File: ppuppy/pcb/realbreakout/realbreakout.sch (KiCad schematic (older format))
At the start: 6 parts, among them J1 Conn_01x36, J2 Conn_01x36, J3 Conn_01x36, U1 nescartheader, U2 piheader

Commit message: More notes, work on breakout; add gpio 'direct access' code that is supposedly faster than bcm lib (but actually it appears to use the same approach, maybe without memory barrier)?
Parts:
- added U?: nescic, symbol nescic
- E1: renamed from E?; footprint (none) -> Housings_DIP:DIP-32_W15.24mm
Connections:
- net 5V: now also U?.16 (5V)
- net GND: now also U?.11 (GND/RESET_A), U?.12 (GND/RESET_B), U?.13 (GND), U?.14 (GND), U?.15 (GND), U?.3 (SEED), U?.4 (LOCK_KEY), U?.8 (GND)
- net at J1.34 (Pin_34), U1.34 (CIC_toPak): now also U?.2 (DATA_IN)
- net at J1.35 (Pin_35), U1.35 (CIC_toMB): now also U?.1 (DATA_OUT)
- net at J2.3 (Pin_3), J3.3 (Pin_3), U1.70 (/CIC_RST): now also U?.7 (RESET)
- net at J2.2 (Pin_2), J3.2 (Pin_2), U1.71 (CIC_CLK): now also U?.6 (CLK)

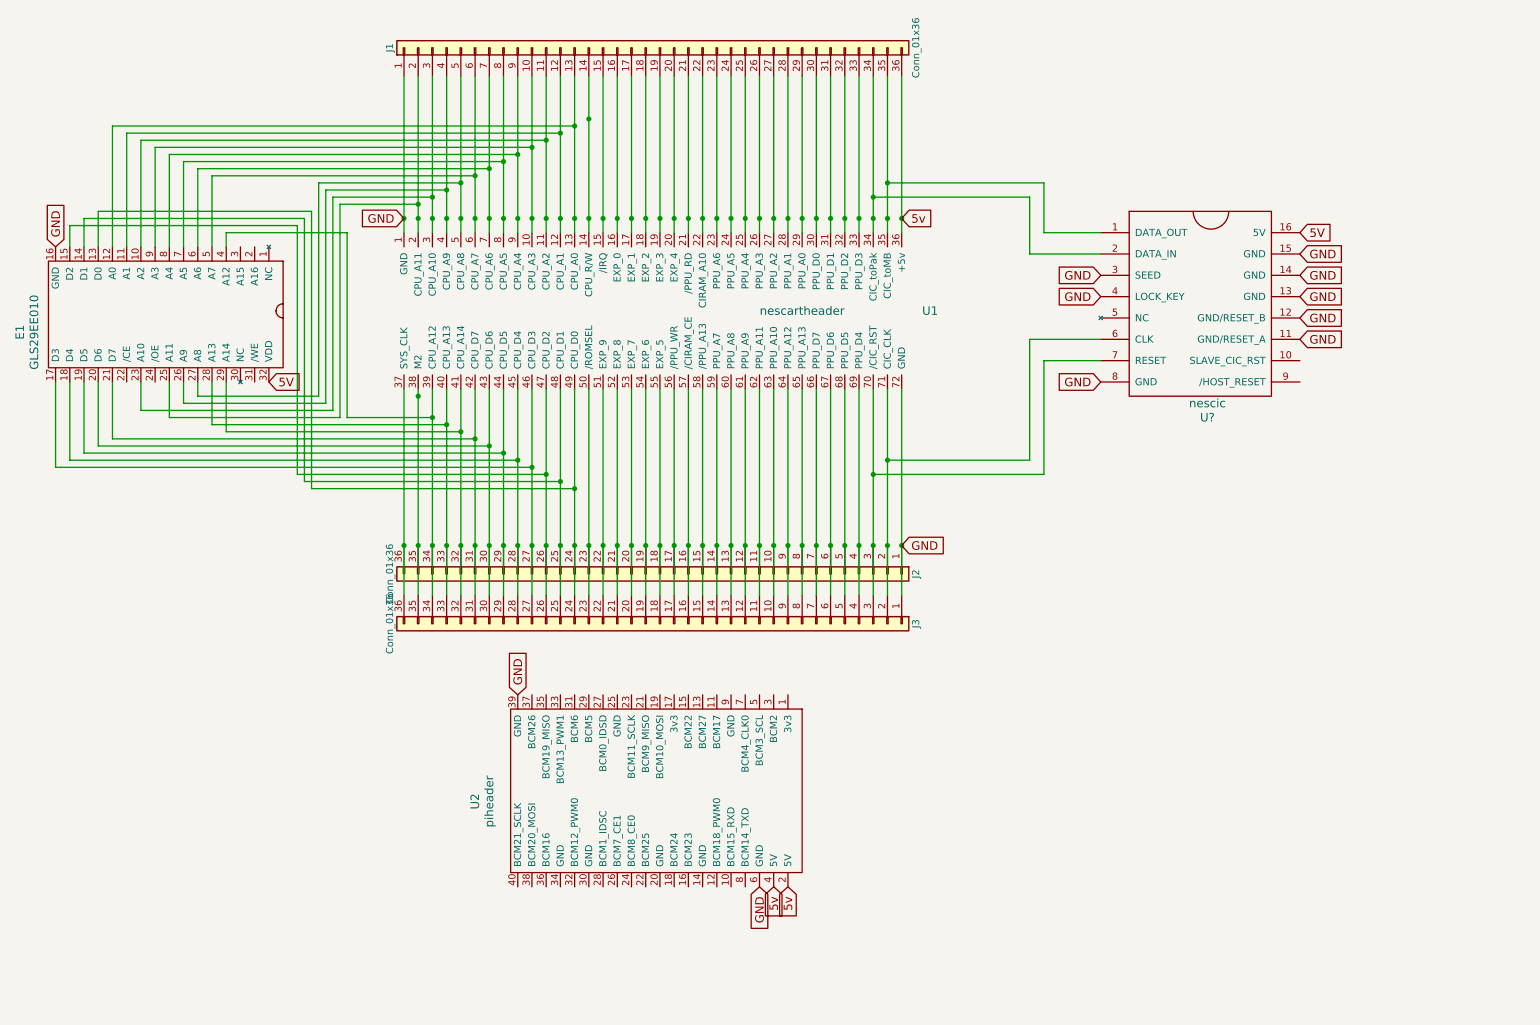
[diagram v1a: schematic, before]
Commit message: Almost ready PCB, longer lead-in in cart knock
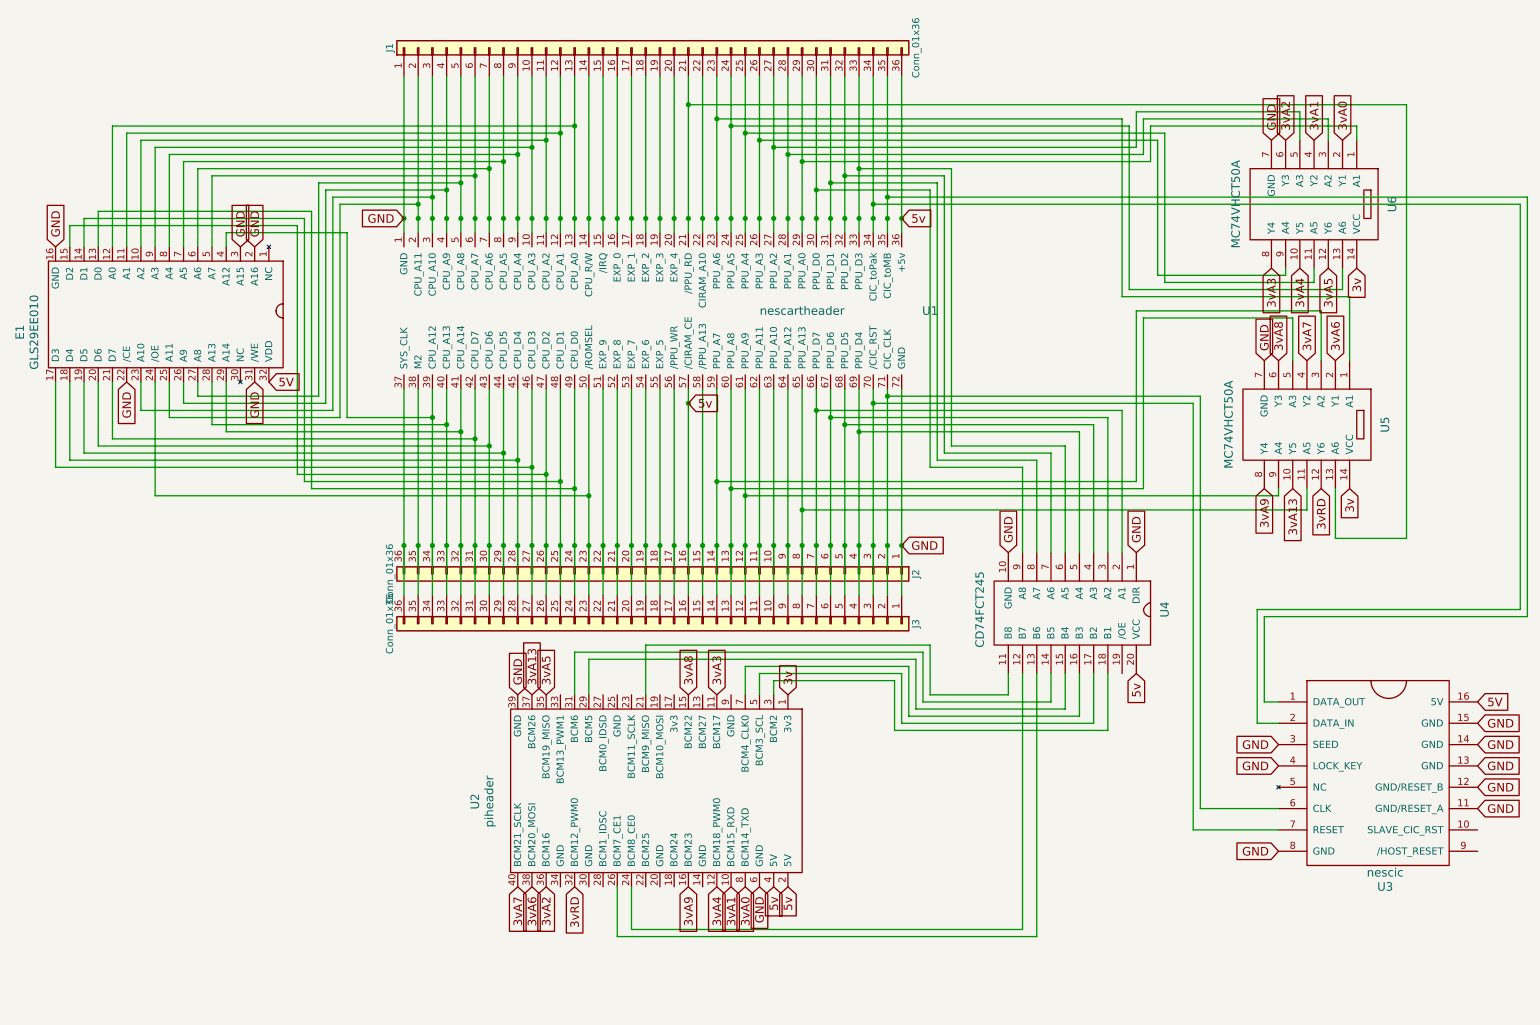
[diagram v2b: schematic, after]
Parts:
- added U4: CD74FCT245, Housings_DIP:DIP-20_W7.62mm, symbol CD74FCT245
- added U5, U6: MC74VHCT50A, Housings_SOIC:SOIC-14_3.9x8.7mm_Pitch1.27mm, symbol MC74VHCT50A
- U3: renamed from U?; footprint (none) -> Housings_DIP:DIP-16_W7.62mm
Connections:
- net 5v: now also J2.16 (Pin_16), J3.16 (Pin_16), U1.57 (/CIRAM_CE), U4.20 (VCC)
- net GND: now also E1.2 (A16), E1.22 (/CE), E1.3 (A15), E1.31 (/WE), U4.1 (DIR), U4.10 (GND), U5.7 (GND), U6.7 (GND)
- net at J1.21 (Pin_21), U1.21 (/PPU_RD): now also U5.13 (A6)
- net at J1.23 (Pin_23), U1.23 (PPU_A6): now also U5.1 (A1)
- net at J1.24 (Pin_24), U1.24 (PPU_A5): now also U6.13 (A6)
- net at J1.25 (Pin_25), U1.25 (PPU_A4): now also U6.11 (A5)
- net at J1.26 (Pin_26), U1.26 (PPU_A3): now also U6.9 (A4)
- net at J1.27 (Pin_27), U1.27 (PPU_A2): now also U6.5 (A3)
- net at J1.28 (Pin_28), U1.28 (PPU_A1): now also U6.3 (A2)
- net at J1.29 (Pin_29), U1.29 (PPU_A0): now also U6.1 (A1)
- net at J1.30 (Pin_30), U1.30 (PPU_D0): now also U4.9 (A8)
- net at J1.31 (Pin_31), U1.31 (PPU_D1): now also U4.8 (A7)
- net at J1.32 (Pin_32), U1.32 (PPU_D2): now also U4.7 (A6)
- net at J1.33 (Pin_33), U1.33 (PPU_D3): now also U4.6 (A5)
- net at J2.23 (Pin_23), J3.23 (Pin_23), U1.50 (/ROMSEL): now also E1.24 (/OE)
- net at J2.14 (Pin_14), J3.14 (Pin_14), U1.59 (PPU_A7): now also U5.3 (A2)
- net at J2.13 (Pin_13), J3.13 (Pin_13), U1.60 (PPU_A8): now also U5.5 (A3)
- net at J2.12 (Pin_12), J3.12 (Pin_12), U1.61 (PPU_A9): now also U5.9 (A4)
- net at J2.8 (Pin_8), J3.8 (Pin_8), U1.65 (PPU_A13): now also U5.11 (A5)
- net at J2.7 (Pin_7), J3.7 (Pin_7), U1.66 (PPU_D7): now also U4.2 (A1)
- net at J2.6 (Pin_6), J3.6 (Pin_6), U1.67 (PPU_D6): now also U4.3 (A2)
- net at J2.5 (Pin_5), J3.5 (Pin_5), U1.68 (PPU_D5): now also U4.4 (A3)
- net at J2.4 (Pin_4), J3.4 (Pin_4), U1.69 (PPU_D4): now also U4.5 (A4)
- net 3v: now reaches U2.1 (3v3)
- net 3v: now also U5.14 (VCC), U6.14 (VCC)
- net 3vA1: now reaches U2.10 (BCM15_RXD)
- net 3vA1: now also U6.4 (Y2)
- net 3vA3: now reaches U2.11 (BCM17)
- net 3vA3: now also U6.8 (Y4)
- net 3vA4: now reaches U2.12 (BCM18_PWM0)
- net 3vA4: now also U6.10 (Y5)
- net 3vA8: now reaches U2.15 (BCM22)
- net 3vA8: now also U5.6 (Y3)
- net 3vA9: now reaches U2.16 (BCM23)
- net 3vA9: now also U5.8 (Y4)
- net at U2.21 (BCM9_MISO): now also U4.11 (B8)
- net at U2.24 (BCM8_CE0): now also U4.12 (B7)
- net at U2.26 (BCM7_CE1): now also U4.13 (B6)
- net at U2.29 (BCM5): now also U4.15 (B4)
- net at U2.3 (BCM2): now also U4.18 (B1)
- net at U2.31 (BCM6): now also U4.14 (B5)
- net 3vRD: now reaches U2.32 (BCM12_PWM0)
- net 3vRD: now also U5.12 (Y6)
- net 3vA5: now reaches U2.35 (BCM19_MISO)
- net 3vA5: now also U6.12 (Y6)
- net 3vA2: now reaches U2.36 (BCM16)
- net 3vA2: now also U6.6 (Y3)
- net 3vA13: now reaches U2.37 (BCM26)
- net 3vA13: now also U5.10 (Y5)
- net 3vA6: now reaches U2.38 (BCM20_MOSI)
- net 3vA6: now also U5.2 (Y1)
- net 3vA7: now reaches U2.40 (BCM21_SCLK)
- net 3vA7: now also U5.4 (Y2)
- net at U2.5 (BCM3_SCL): now also U4.17 (B2)
- net at U2.7 (BCM4_CLK0): now also U4.16 (B3)
- net 3vA0: now reaches U2.8 (BCM14_TXD)
- net 3vA0: now also U6.2 (Y1)
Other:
- moved on the sheet: U3

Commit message: This is the version of PCB that I first printed
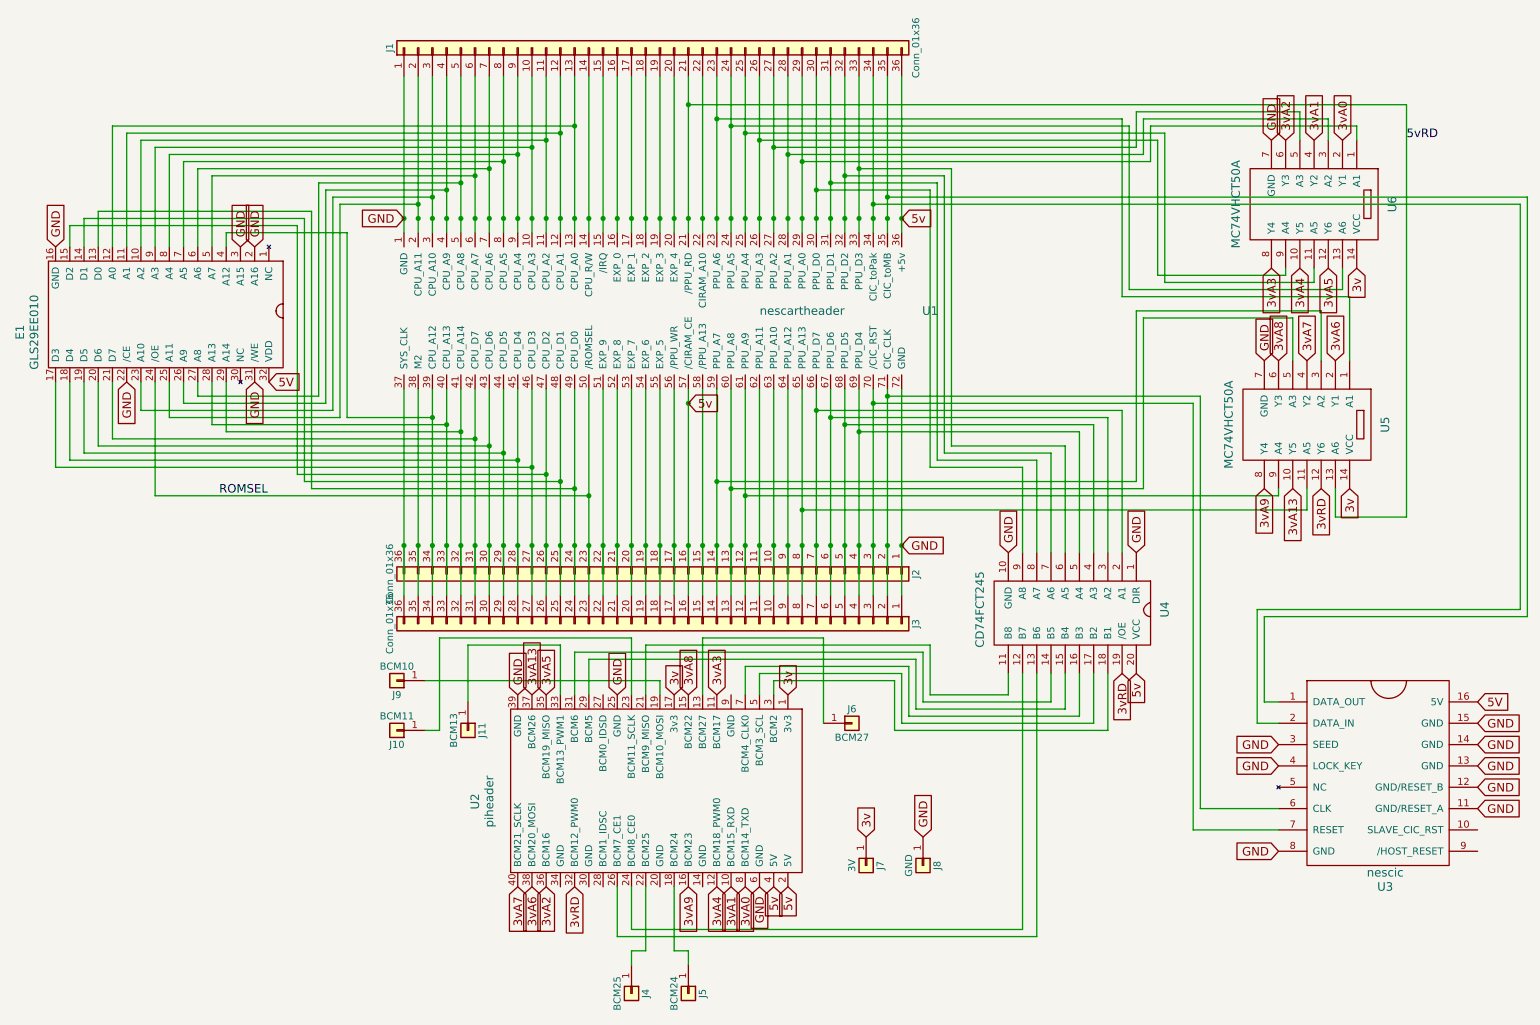
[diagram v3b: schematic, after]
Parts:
- added J10: BCM11, symbol Conn_01x01
- added J11: BCM13, symbol Conn_01x01
- added J4: BCM25, Pin_Headers:Pin_Header_Straight_1x01_Pitch2.54mm, symbol Conn_01x01
- added J5: BCM24, Pin_Headers:Pin_Header_Straight_1x01_Pitch2.54mm, symbol Conn_01x01
- added J6: BCM27, Pin_Headers:Pin_Header_Straight_1x01_Pitch2.54mm, symbol Conn_01x01
- added J7: 3V, Pin_Headers:Pin_Header_Straight_1x01_Pitch2.54mm, symbol Conn_01x01
- added J8: GND, Pin_Headers:Pin_Header_Straight_1x01_Pitch2.54mm, symbol Conn_01x01
- added J9: BCM10, symbol Conn_01x01
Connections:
- net 3v: now also U2.17 (3v3), J7.1 (Pin_1)
- net 3vRD: now also U4.19 (/OE)
- net GND: now also U2.25 (GND), J8.1 (Pin_1)
- net 5vRD: now reaches J1.21 (Pin_21), U1.21 (/PPU_RD), U5.13 (A6)
- net ROMSEL: now reaches E1.24 (/OE), J2.23 (Pin_23), J3.23 (Pin_23), U1.50 (/ROMSEL)
- net at U2.13 (BCM27): now also J6.1 (Pin_1)
- net at U2.18 (BCM24): now also J5.1 (Pin_1)
- net at U2.19 (BCM10_MOSI): now also J9.1 (Pin_1)
- net at U2.22 (BCM25): now also J4.1 (Pin_1)
- net at U2.23 (BCM11_SCLK): now also J10.1 (Pin_1)
- net at U2.33 (BCM13_PWM1): now also J11.1 (Pin_1)
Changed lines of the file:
@@
 Wire Wire Line
 	5200 550  10250 550
-Wire Wire Line
-	10250 550  10250 3600
-Wire Wire Line
-	10250 3600 9750 3600
-Wire Wire Line
-	9750 3600 9750 3250
 Text GLabel 9650 3250 3    60   Input ~ 0
 3vRD
@@
 Text GLabel 5200 2650 2    60   Input ~ 0
 5v
+Text GLabel 4700 4700 1    60   Input ~ 0
+GND
+Text GLabel 5100 4700 1    60   Input ~ 0
+3v
+Text GLabel 8250 4550 3    60   Input ~ 0
+3vRD
+Wire Wire Line
+	10250 550  10250 3450
+Wire Wire Line
+	10250 3450 9750 3450
+Wire Wire Line
+	9750 3450 9750 3250
+Text Label 10250 800  0    60   ~ 0
+5vRD
+Text Label 1900 3300 0    60   ~ 0
+ROMSEL
+$Comp
+L Conn_01x01 J5
+U 1 1 5ADD43A7
+P 5200 6800
+F 0 "J5" H 5200 6900 50  0000 C CNN
+F 1 "BCM24" H 5200 6700 50  0000 C CNN
+F 2 "Pin_Headers:Pin_Header_Straight_1x01_Pitch2.54mm" H 5200 6800 50  0001 C CNN
+F 3 "" H 5200 6800 50  0001 C CNN
+	1    5200 6800
+	0    1    1    0
+$EndComp
+$Comp
+L Conn_01x01 J4
+U 1 1 5ADD45DE
+P 4800 6800
+F 0 "J4" H 4800 6900 50  0000 C CNN
+F 1 "BCM25" H 4800 6700 50  0000 C CNN
+F 2 "Pin_Headers:Pin_Header_Straight_1x01_Pitch2.54mm" H 4800 6800 50  0001 C CNN
+F 3 "" H 4800 6800 50  0001 C CNN
+	1    4800 6800
+	0    1    1    0
+$EndComp
+Wire Wire Line
+	4900 6050 4900 6500
+Wire Wire Line
+	4900 6500 4800 6500
+Wire Wire Line
+	4800 6500 4800 6600
+Wire Wire Line
+	5100 6050 5100 6500
+Wire Wire Line
+	5100 6500 5200 6500
+Wire Wire Line
+	5200 6500 5200 6600
+$Comp
+L Conn_01x01 J6
+U 1 1 5ADD4C20
+P 6350 4900
+F 0 "J6" H 6350 5000 50  0000 C CNN
+F 1 "BCM27" H 6350 4800 50  0000 C CNN
+F 2 "Pin_Headers:Pin_Header_Straight_1x01_Pitch2.54mm" H 6350 4900 50  0001 C CNN
+F 3 "" H 6350 4900 50  0001 C CNN
+	1    6350 4900
+	1    0    0    -1
+$EndComp
+Wire Wire Line
+	6150 4900 6150 4300
+Wire Wire Line
+	6150 4300 5300 4300
+Wire Wire Line
+	5300 4300 5300 4700
+$Comp
+L Conn_01x01 J7
+U 1 1 5ADD4DE4
+P 6450 5900
+F 0 "J7" H 6450 6000 50  0000 C CNN
+F 1 "3V" H 6450 5800 50  0000 C CNN
+F 2 "Pin_Headers:Pin_Header_Straight_1x01_Pitch2.54mm" H 6450 5900 50  0001 C CNN
+F 3 "" H 6450 5900 50  0001 C CNN
+	1    6450 5900
+	0    1    1    0
+$EndComp
+$Comp
+L Conn_01x01 J8
+U 1 1 5ADD4E5F
+P 6850 5900
+F 0 "J8" H 6850 6000 50  0000 C CNN
+F 1 "GND" H 6850 5800 50  0000 C CNN
+F 2 "Pin_Headers:Pin_Header_Straight_1x01_Pitch2.54mm" H 6850 5900 50  0001 C CNN
+F 3 "" H 6850 5900 50  0001 C CNN
+	1    6850 5900
+	0    1    1    0
+$EndComp
+Text GLabel 6850 5700 1    60   Input ~ 0
+GND
+Text GLabel 6450 5700 1    60   Input ~ 0
+3v
+$Comp
+L Conn_01x01 J11
+U 1 1 5ADD5E6F
+P 3650 4950
+F 0 "J11" H 3650 5050 50  0000 C CNN
+F 1 "BCM13" H 3650 4850 50  0000 C CNN
+F 2 "" H 3650 4950 50  0001 C CNN
+F 3 "" H 3650 4950 50  0001 C CNN
+	1    3650 4950
+	0    1    1    0
+$EndComp
+Wire Wire Line
+	3650 4750 3650 4350
+Wire Wire Line
+	3650 4350 4300 4350
+Wire Wire Line
+	4300 4350 4300 4700
+$Comp
+L Conn_01x01 J9
+U 1 1 5ADD629E
+P 3150 4600
+F 0 "J9" H 3150 4700 50  0000 C CNN
+F 1 "BCM10" H 3150 4500 50  0000 C CNN
+F 2 "" H 3150 4600 50  0001 C CNN
+F 3 "" H 3150 4600 50  0001 C CNN
+	1    3150 4600
+	-1   0    0    1
+$EndComp
+$Comp
+L Conn_01x01 J10
+U 1 1 5ADD6490
+P 3150 4950
+F 0 "J10" H 3150 5050 50  0000 C CNN
+F 1 "BCM11" H 3150 4850 50  0000 C CNN
+F 2 "" H 3150 4950 50  0001 C CNN
+F 3 "" H 3150 4950 50  0001 C CNN
+	1    3150 4950
+	-1   0    0    1
+$EndComp
+Wire Wire Line
+	3350 4950 3450 4950
+Wire Wire Line
+	3450 4950 3450 4300
+Wire Wire Line
+	3450 4300 4800 4300
+Wire Wire Line
+	4800 4300 4800 4700
+Wire Wire Line
+	3350 4600 5000 4600
+Wire Wire Line
+	5000 4600 5000 4700
 $EndSCHEMATC

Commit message: v2 of board
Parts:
- J10, J11, J9: footprint (none) -> Pin_Headers:Pin_Header_Straight_1x01_Pitch2.54mm
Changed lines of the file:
@@
 F 0 "J11" H 3650 5050 50  0000 C CNN
 F 1 "BCM13" H 3650 4850 50  0000 C CNN
-F 2 "" H 3650 4950 50  0001 C CNN
+F 2 "Pin_Headers:Pin_Header_Straight_1x01_Pitch2.54mm" H 3650 4950 50  0001 C CNN
 F 3 "" H 3650 4950 50  0001 C CNN
 	1    3650 4950
@@
 F 0 "J9" H 3150 4700 50  0000 C CNN
 F 1 "BCM10" H 3150 4500 50  0000 C CNN
-F 2 "" H 3150 4600 50  0001 C CNN
+F 2 "Pin_Headers:Pin_Header_Straight_1x01_Pitch2.54mm" H 3150 4600 50  0001 C CNN
 F 3 "" H 3150 4600 50  0001 C CNN
 	1    3150 4600
@@
 F 0 "J10" H 3150 5050 50  0000 C CNN
 F 1 "BCM11" H 3150 4850 50  0000 C CNN
-F 2 "" H 3150 4950 50  0001 C CNN
+F 2 "Pin_Headers:Pin_Header_Straight_1x01_Pitch2.54mm" H 3150 4950 50  0001 C CNN
 F 3 "" H 3150 4950 50  0001 C CNN
 	1    3150 4950
